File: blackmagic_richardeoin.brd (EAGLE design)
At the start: 55 x 18 mm, 52 parts, among them IC1 STM32F_48PIN, IC2 TXS0108, IC3 TLV70033DCK, IC4 IP4220CZ6, IC5 IP4220CZ6, Q1 IRLML5103, U1 AD8655ARMZ, U3 LT1763CDEPBF

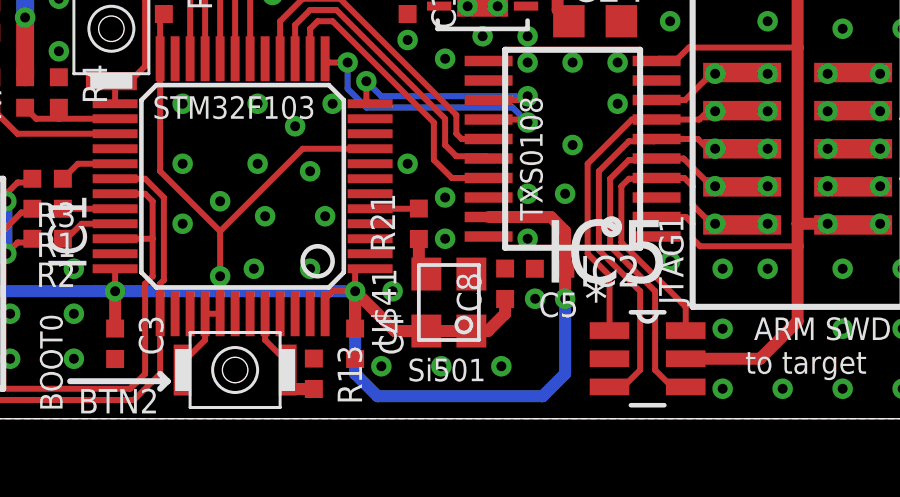
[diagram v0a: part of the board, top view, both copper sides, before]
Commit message: Update parts list with 2x esd, split passives into separte list for clarity
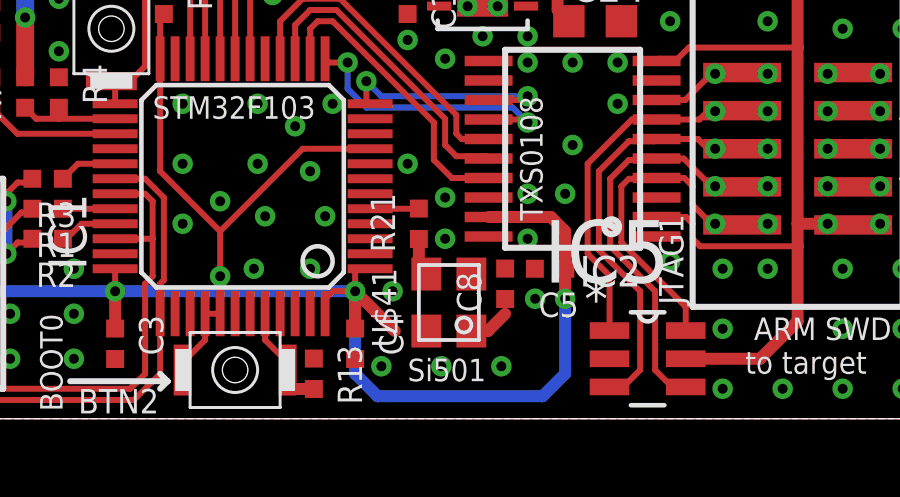
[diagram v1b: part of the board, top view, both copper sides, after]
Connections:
- new net IC8: C8.1, U$41.4
- net 3.3V: no longer C8.1, U$41.4
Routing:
- net 3.3V: track 86.0 -> 82.9 mm
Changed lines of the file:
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@@
 <?xml version="1.0" encoding="utf-8"?>
 <!DOCTYPE eagle SYSTEM "eagle.dtd">
-<eagle version="7.3.0">
+<eagle version="6.5.0">
 <drawing>
 <settings>
@@
 <layer number="22" name="bPlace" color="7" fill="1" visible="yes" active="yes"/>
 <layer number="23" name="tOrigins" color="15" fill="1" visible="yes" active="yes"/>
-<layer number="24" name="bOrigins" color="15" fill="1" visible="no" active="yes"/>
+<layer number="24" name="bOrigins" color="15" fill="1" visible="yes" active="yes"/>
 <layer number="25" name="tNames" color="7" fill="1" visible="yes" active="yes"/>
-<layer number="26" name="bNames" color="7" fill="1" visible="no" active="yes"/>
-<layer number="27" name="tValues" color="7" fill="1" visible="no" active="yes"/>
-<layer number="28" name="bValues" color="7" fill="1" visible="no" active="yes"/>
+<layer number="26" name="bNames" color="7" fill="1" visible="yes" active="yes"/>
+<layer number="27" name="tValues" color="7" fill="1" visible="yes" active="yes"/>
+<layer number="28" name="bValues" color="7" fill="1" visible="yes" active="yes"/>
 <layer number="29" name="tStop" color="7" fill="3" visible="yes" active="yes"/>
 <layer number="30" name="bStop" color="7" fill="6" visible="yes" active="yes"/>
 <layer number="31" name="tCream" color="7" fill="4" visible="yes" active="yes"/>
-<layer number="32" name="bCream" color="7" fill="5" visible="no" active="yes"/>
+<layer number="32" name="bCream" color="7" fill="5" visible="yes" active="yes"/>
 <layer number="33" name="tFinish" color="6" fill="3" visible="yes" active="yes"/>
 <layer number="34" name="bFinish" color="6" fill="6" visible="yes" active="yes"/>
@@
 <pass name="Default">
 <param name="RoutingGrid" value="50mil"/>
-<param name="AutoGrid" value="1"/>
-<param name="Efforts" value="0"/>
-<param name="TopRouterVariant" value="1"/>
 <param name="tpViaShape" value="round"/>
 <param name="PrefDir.1" value="|"/>
@@
 <contactref element="JTAG2" pad="1"/>
 <contactref element="R15" pad="2"/>
-<contactref element="U$41" pad="4"/>
-<contactref element="C8" pad="1"/>
 <contactref element="U$41" pad="1"/>
-<wire x1="38.125" y1="2.925" x2="39.625" y2="2.925" width="0.4" layer="1"/>
 <wire x1="40.2" y1="6.725" x2="42.275" y2="6.725" width="0.4" layer="1"/>
 <wire x1="42.275" y1="6.725" x2="42.75" y2="6.25" width="0.4" layer="1"/>
@@
 <wire x1="39.625" y1="2.925" x2="40.175" y2="2.925" width="0.4" layer="1"/>
 <wire x1="40.175" y1="2.925" x2="40.75" y2="3.5" width="0.4" layer="1"/>
-<wire x1="40.75" y1="3.5" x2="40.75" y2="3.992" width="0.4" layer="1"/>
 <via x="42.75" y="4" extent="1-16" drill="0.3302"/>
 <wire x1="42.75" y1="5.008" x2="42.75" y2="4" width="0.4" layer="1"/>
 <wire x1="35.75" y1="4.25" x2="37.075" y2="2.925" width="0.4" layer="1"/>
-<wire x1="37.075" y1="2.925" x2="38.125" y2="2.925" width="0.4" layer="1"/>
 <wire x1="35.75" y1="3.008" x2="35.75" y2="4.25" width="0.4" layer="1"/>
 <wire x1="30.75" y1="3.5" x2="30.75" y2="2.625" width="0.2" layer="1"/>
@@
 <wire x1="29.25" y1="12" x2="29.25" y2="13.367" width="0.2" layer="1"/>
 <wire x1="29.25" y1="13.367" x2="29.375" y2="13.492" width="0.2" layer="1"/>
+<wire x1="42.75" y1="4" x2="40.75" y2="3.5" width="0" layer="19" extent="1-1"/>
 </signal>
 <signal name="N$24">
@@
 <via x="53.25" y="10.25" extent="1-16" drill="0.3302"/>
 </signal>
+<signal name="IC8">
+<contactref element="C8" pad="1"/>
+<contactref element="U$41" pad="4"/>
+<wire x1="38.125" y1="2.925" x2="40.75" y2="3.992" width="0" layer="19" extent="1-1"/>
+</signal>
 </signals>
